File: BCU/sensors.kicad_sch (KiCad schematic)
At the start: 1 part

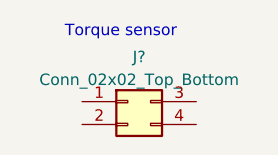
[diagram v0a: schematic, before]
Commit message: Make rough component placement for evaluating missing 3D
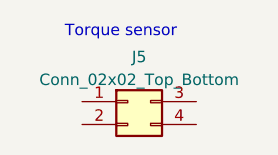
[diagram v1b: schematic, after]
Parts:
- gave numbers to parts that had none: 1
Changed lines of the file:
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@@
   (symbol (lib_id "Connector_Generic:Conn_02x02_Top_Bottom") (at 133.985 102.87 0) (unit 1)
     (in_bom yes) (on_board yes) (fields_autoplaced)
-    (property "Reference" "J?" (id 0) (at 135.255 97.9002 0))
+    (property "Reference" "J5" (id 0) (at 135.255 97.9002 0))
     (property "Value" "Conn_02x02_Top_Bottom" (id 1) (at 135.255 100.4371 0))
     (property "Footprint" "" (id 2) (at 133.985 102.87 0)
